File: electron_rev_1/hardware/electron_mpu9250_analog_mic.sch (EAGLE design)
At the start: 43 parts, among them IC2 S25FL128SAGNFI011, IC4 MIC_I2S_SPH0645, U1 MPU-9250, U10 GAS_SENSOR, U2 Value, U3 OPA322AIDBVT, U4 microSD, U5 +12v, U6 +12v, U7 GAS_SENSOR

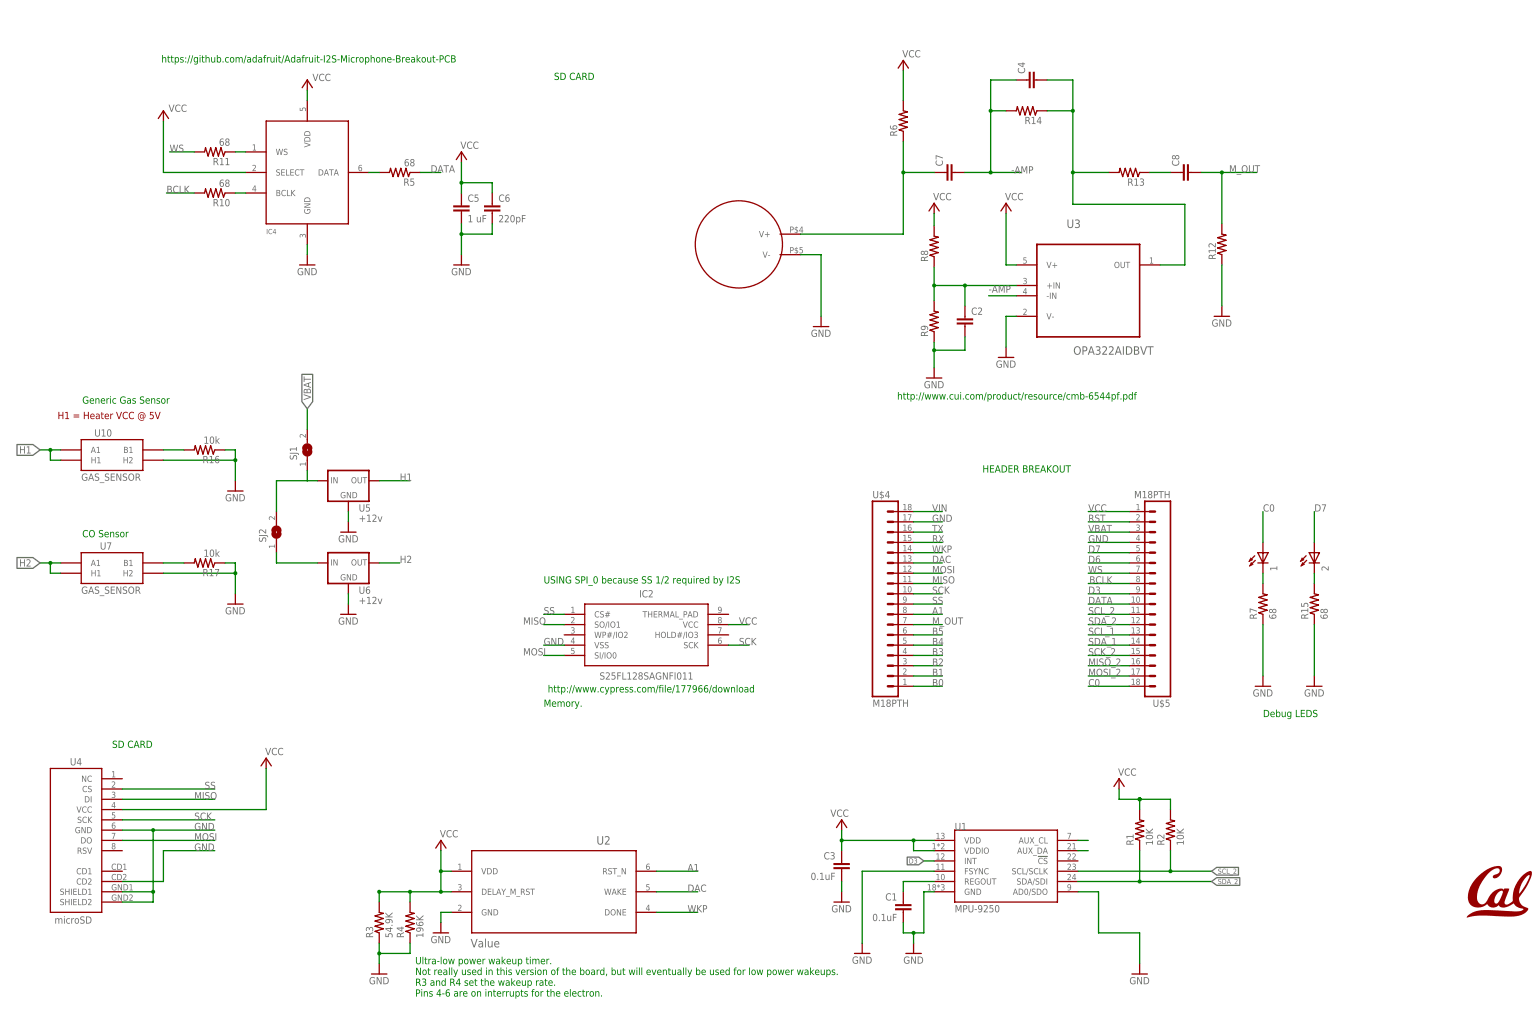
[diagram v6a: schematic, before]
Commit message: mainly cosmetic changes to schematic. changed label types
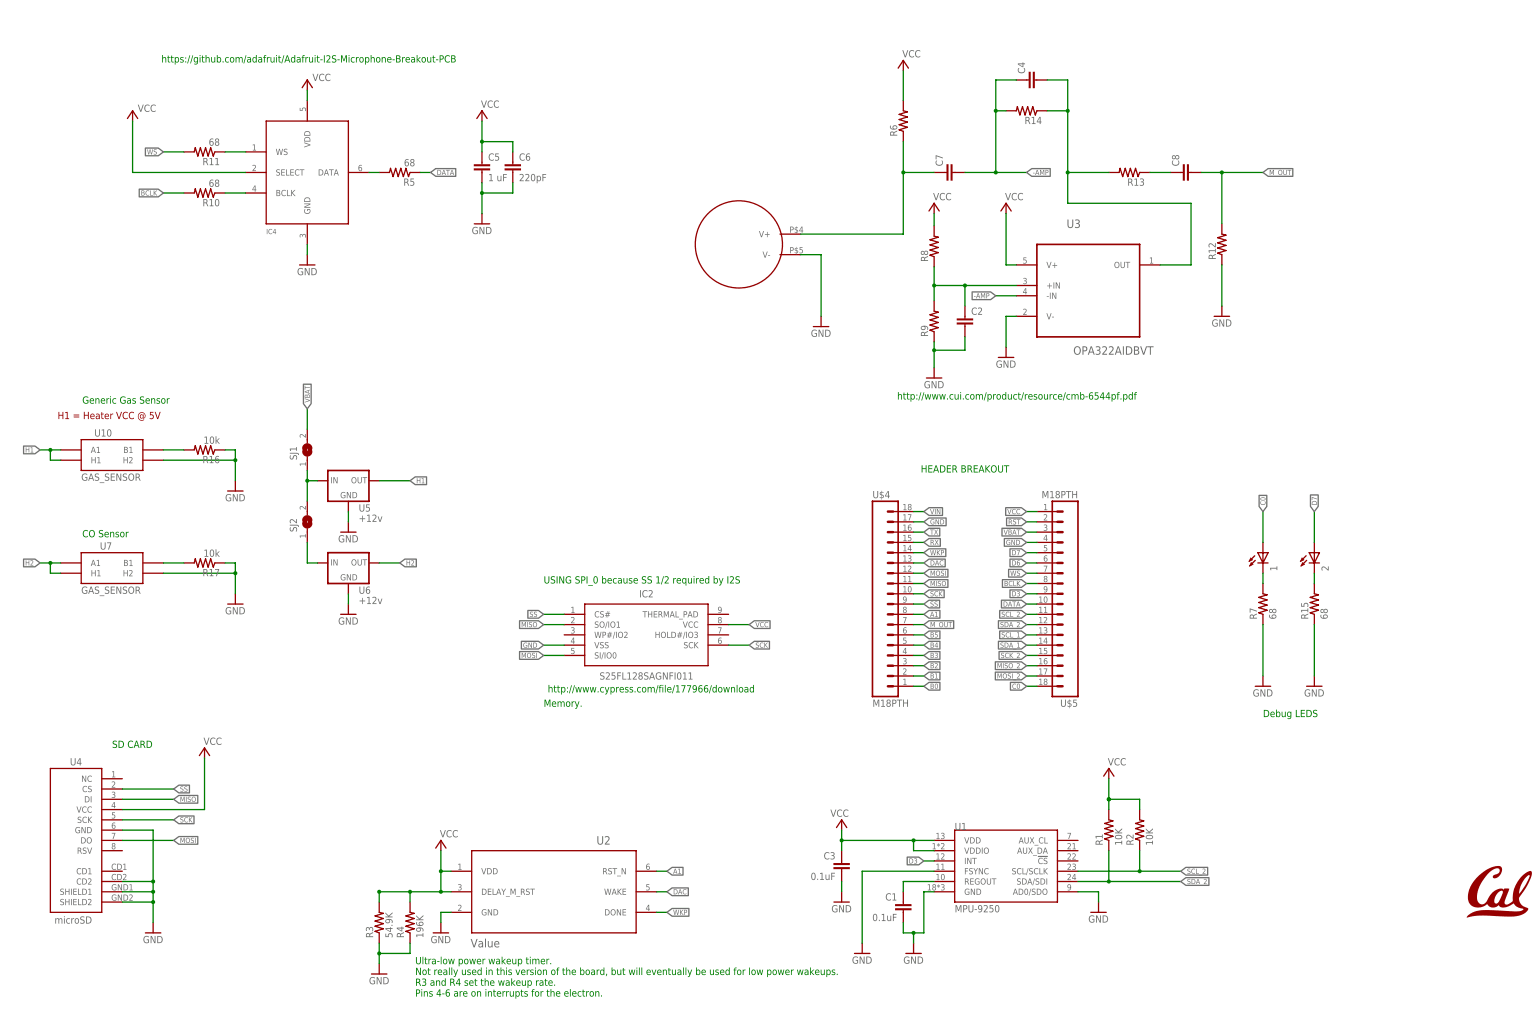
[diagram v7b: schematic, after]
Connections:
- removed net AUX_CL: U1.AUX_CL
- removed net AUX_DA: U1.AUX_DA
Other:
- moved on the sheet: C5, C6, R1, R10, R11, R2, SJ2, U$5

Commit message: cosmetic changes
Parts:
- C2, C8: value (none) -> 2.2uF
- C4: value (none) -> 16pF
- C7: value (none) -> 25uF
- R12, R8, R9: value (none) -> 100K
- R13: value (none) -> 49.9
- R14: value (none) -> 75K
- R15, R7: value 68 -> (none)
- R6: value (none) -> 13.7K
- U5, U6: value +12v -> +5v
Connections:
- new net N$10: SJ1.1, SJ2.2, U5.IN
- net VBAT: no longer SJ1.1, SJ2.2, U5.IN
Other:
- note added: "ANALOG MIC"
- note added: "DEBUG"
- note added: "DIGITAL MIC"
- note added: "ELECTRON"
- note added: "GAS"
- note added: "IMU"
- note added: "MEM"
- note added: "TIMER"
- note removed: "Generic Gas Sensor"
- note removed: "HEADER BREAKOUT"
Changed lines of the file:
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@@
 <part name="R2" library="SparkFun-Resistors" deviceset="10KOHM-1/10W-1%(0603)" device="0603" value="10K"/>
 <part name="U$1" library="microphone" deviceset="CMB-6544PF" device=""/>
-<part name="R6" library="resistor" library_urn="urn:adsk.eagle:library:348" deviceset="R-US_" device="R0603" package3d_urn="urn:adsk.eagle:package:26057/1"/>
-<part name="C2" library="resistor" library_urn="urn:adsk.eagle:library:348" deviceset="C-EU" device="C0603" package3d_urn="urn:adsk.eagle:package:26138/1"/>
-<part name="R8" library="resistor" library_urn="urn:adsk.eagle:library:348" deviceset="R-US_" device="R0603" package3d_urn="urn:adsk.eagle:package:26057/1"/>
-<part name="R9" library="resistor" library_urn="urn:adsk.eagle:library:348" deviceset="R-US_" device="R0603" package3d_urn="urn:adsk.eagle:package:26057/1"/>
-<part name="R12" library="resistor" library_urn="urn:adsk.eagle:library:348" deviceset="R-US_" device="R0603" package3d_urn="urn:adsk.eagle:package:26057/1"/>
-<part name="R13" library="resistor" library_urn="urn:adsk.eagle:library:348" deviceset="R-US_" device="R0603" package3d_urn="urn:adsk.eagle:package:26057/1"/>
-<part name="R14" library="resistor" library_urn="urn:adsk.eagle:library:348" deviceset="R-US_" device="R0603" package3d_urn="urn:adsk.eagle:package:26057/1"/>
-<part name="C4" library="resistor" library_urn="urn:adsk.eagle:library:348" deviceset="C-EU" device="C0603" package3d_urn="urn:adsk.eagle:package:26138/1"/>
-<part name="C7" library="resistor" library_urn="urn:adsk.eagle:library:348" deviceset="C-EU" device="C0603" package3d_urn="urn:adsk.eagle:package:26138/1"/>
+<part name="R6" library="resistor" library_urn="urn:adsk.eagle:library:348" deviceset="R-US_" device="R0603" package3d_urn="urn:adsk.eagle:package:26057/1" value="13.7K"/>
+<part name="C2" library="resistor" library_urn="urn:adsk.eagle:library:348" deviceset="C-EU" device="C0603" package3d_urn="urn:adsk.eagle:package:26138/1" value="2.2uF"/>
+<part name="R8" library="resistor" library_urn="urn:adsk.eagle:library:348" deviceset="R-US_" device="R0603" package3d_urn="urn:adsk.eagle:package:26057/1" value="100K"/>
+<part name="R9" library="resistor" library_urn="urn:adsk.eagle:library:348" deviceset="R-US_" device="R0603" package3d_urn="urn:adsk.eagle:package:26057/1" value="100K"/>
+<part name="R12" library="resistor" library_urn="urn:adsk.eagle:library:348" deviceset="R-US_" device="R0603" package3d_urn="urn:adsk.eagle:package:26057/1" value="100K"/>
+<part name="R13" library="resistor" library_urn="urn:adsk.eagle:library:348" deviceset="R-US_" device="R0603" package3d_urn="urn:adsk.eagle:package:26057/1" value="49.9"/>
+<part name="R14" library="resistor" library_urn="urn:adsk.eagle:library:348" deviceset="R-US_" device="R0603" package3d_urn="urn:adsk.eagle:package:26057/1" value="75K"/>
+<part name="C4" library="resistor" library_urn="urn:adsk.eagle:library:348" deviceset="C-EU" device="C0603" package3d_urn="urn:adsk.eagle:package:26138/1" value="16pF"/>
+<part name="C7" library="resistor" library_urn="urn:adsk.eagle:library:348" deviceset="C-EU" device="C0603" package3d_urn="urn:adsk.eagle:package:26138/1" value="25uF"/>
 <part name="GND4" library="supply1" library_urn="urn:adsk.eagle:library:371" deviceset="GND" device=""/>
 <part name="GND5" library="supply1" library_urn="urn:adsk.eagle:library:371" deviceset="GND" device=""/>
 <part name="GND6" library="supply1" library_urn="urn:adsk.eagle:library:371" deviceset="GND" device=""/>
-<part name="C8" library="resistor" library_urn="urn:adsk.eagle:library:348" deviceset="C-EU" device="C0603" package3d_urn="urn:adsk.eagle:package:26138/1"/>
+<part name="C8" library="resistor" library_urn="urn:adsk.eagle:library:348" deviceset="C-EU" device="C0603" package3d_urn="urn:adsk.eagle:package:26138/1" value="2.2uF"/>
 <part name="GND8" library="supply1" library_urn="urn:adsk.eagle:library:371" deviceset="GND" device=""/>
 <part name="P+1" library="supply1" library_urn="urn:adsk.eagle:library:371" deviceset="VCC" device=""/>
@@
 <part name="1" library="adafruit" library_urn="urn:adsk.eagle:library:420" deviceset="LED" device="CHIP-LED0603"/>
 <part name="GND13" library="SparkFun-Aesthetics" deviceset="GND" device=""/>
-<part name="R7" library="resistor" library_urn="urn:adsk.eagle:library:348" deviceset="R-US_" device="R0603" package3d_urn="urn:adsk.eagle:package:26057/1" value="68"/>
+<part name="R7" library="resistor" library_urn="urn:adsk.eagle:library:348" deviceset="R-US_" device="R0603" package3d_urn="urn:adsk.eagle:package:26057/1"/>
 <part name="2" library="adafruit" library_urn="urn:adsk.eagle:library:420" deviceset="LED" device="CHIP-LED0603"/>
 <part name="GND14" library="SparkFun-Aesthetics" deviceset="GND" device=""/>
-<part name="R15" library="resistor" library_urn="urn:adsk.eagle:library:348" deviceset="R-US_" device="R0603" package3d_urn="urn:adsk.eagle:package:26057/1" value="68"/>
+<part name="R15" library="resistor" library_urn="urn:adsk.eagle:library:348" deviceset="R-US_" device="R0603" package3d_urn="urn:adsk.eagle:package:26057/1"/>
 <part name="U4" library="SparkFun" deviceset="USD-SOCKET" device="SMD" value="microSD"/>
 <part name="U7" library="SparkFun" deviceset="GAS_SENSOR" device=""/>
@@
 <part name="GND16" library="supply1" library_urn="urn:adsk.eagle:library:371" deviceset="GND" device=""/>
 <part name="FRAME1" library="frames" library_urn="urn:adsk.eagle:library:229" deviceset="A3L-LOC" device=""/>
-<part name="U5" library="SparkFun-IC-Power" library_urn="urn:adsk.eagle:library:526" deviceset="V_REG_78XX" device="7812" package3d_urn="urn:adsk.eagle:package:39067/1" value="+12v"/>
-<part name="U6" library="SparkFun-IC-Power" library_urn="urn:adsk.eagle:library:526" deviceset="V_REG_78XX" device="7812" package3d_urn="urn:adsk.eagle:package:39067/1" value="+12v"/>
+<part name="U5" library="SparkFun-IC-Power" library_urn="urn:adsk.eagle:library:526" deviceset="V_REG_78XX" device="7812" package3d_urn="urn:adsk.eagle:package:39067/1" value="+5v"/>
+<part name="U6" library="SparkFun-IC-Power" library_urn="urn:adsk.eagle:library:526" deviceset="V_REG_78XX" device="7812" package3d_urn="urn:adsk.eagle:package:39067/1" value="+5v"/>
 <part name="GND17" library="SparkFun-Aesthetics" deviceset="GND" device=""/>
 <part name="GND18" library="SparkFun-Aesthetics" deviceset="GND" device=""/>
@@
 <text x="210.82" y="43.18" size="1.778" layer="91">Debug LEDS</text>
 <text x="33.02" y="45.72" size="1.778" layer="91">Memory. </text>
-<text x="126.238" y="103.632" size="1.778" layer="91">HEADER BREAKOUT</text>
 <text x="-81.026" y="87.63" size="1.778" layer="91">CO Sensor</text>
-<text x="-73.66" y="35.56" size="1.778" layer="91">SD CARD</text>
 <text x="-87.122" y="116.84" size="1.778" layer="94">H1 = Heater VCC @ 5V</text>
-<text x="-81.026" y="120.65" size="1.778" layer="91">Generic Gas Sensor</text>
+<text x="132.08" y="210.82" size="5.08" layer="91">ANALOG MIC</text>
+<text x="-43.18" y="210.82" size="5.08" layer="91">DIGITAL MIC</text>
+<text x="-48.26" y="124.46" size="5.08" layer="91">GAS</text>
+<text x="50.8" y="83.82" size="5.08" layer="91">MEM</text>
+<text x="-68.58" y="43.18" size="5.08" layer="91">SD CARD</text>
+<text x="22.86" y="15.24" size="5.08" layer="91">TIMER</text>
+<text x="139.7" y="20.32" size="5.08" layer="91">IMU</text>
+<text x="119.38" y="101.6" size="5.08" layer="91">ELECTRON</text>
+<text x="205.74" y="104.14" size="5.08" layer="91">DEBUG</text>
 </plain>
 <instances>
@@
 <pinref part="SJ1" gate="1" pin="2"/>
 </segment>
-<segment>
-<wire x1="-25.4" y1="96.52" x2="-25.4" y2="101.6" width="0.1524" layer="91"/>
-<pinref part="SJ2" gate="1" pin="2"/>
-<pinref part="U5" gate="G$1" pin="IN"/>
-<wire x1="-22.86" y1="101.6" x2="-25.4" y2="101.6" width="0.1524" layer="91"/>
-<pinref part="SJ1" gate="1" pin="1"/>
-<wire x1="-25.4" y1="101.6" x2="-25.4" y2="104.14" width="0.1524" layer="91"/>
-<junction x="-25.4" y="101.6"/>
-</segment>
 </net>
 <net name="D7" class="0">
@@
 </segment>
 </net>
+<net name="N$10" class="0">
+<segment>
+<pinref part="SJ2" gate="1" pin="2"/>
+<pinref part="SJ1" gate="1" pin="1"/>
+<wire x1="-25.4" y1="96.52" x2="-25.4" y2="101.6" width="0.1524" layer="91"/>
+<pinref part="U5" gate="G$1" pin="IN"/>
+<wire x1="-25.4" y1="101.6" x2="-25.4" y2="104.14" width="0.1524" layer="91"/>
+<wire x1="-22.86" y1="101.6" x2="-25.4" y2="101.6" width="0.1524" layer="91"/>
+<junction x="-25.4" y="101.6"/>
+</segment>
+</net>
